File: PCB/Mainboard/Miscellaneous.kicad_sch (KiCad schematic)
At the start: 8 parts

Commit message: Update schematic and lay-out
- Swap out CP2102N, ATmega328PB and CP with new Kicad 6 symbol
- Correct all links to point to new zoudio_symbols and zoudio_footprint libraries
- Lay-out updated, only antenna is left to update.
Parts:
- LOGO1: footprint ZOUDIO-footprints:ZOUDIO25mm_mask -> zoudio_footprints:ZOUDIO25mm_mask
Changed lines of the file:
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@@
     )
     (property "Value" "ZOUDIO" (id 1) (at 172.72 101.6 0))
-    (property "Footprint" "ZOUDIO-footprints:ZOUDIO25mm_mask" (id 2) (at 172.72 95.25 0)
+    (property "Footprint" "zoudio_footprints:ZOUDIO25mm_mask" (id 2) (at 172.72 95.25 0)
       (effects (font (size 1.27 1.27)) hide)
     )

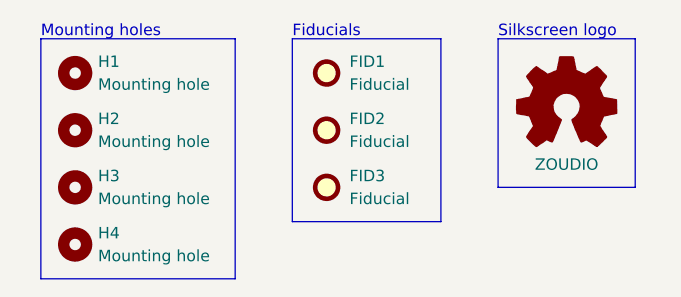
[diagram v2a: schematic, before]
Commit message: Mainboard: version 1.1.1
- No change in electrical connectivity
- Make 3D model more complete
- Improvements in paste layer for manufacturability
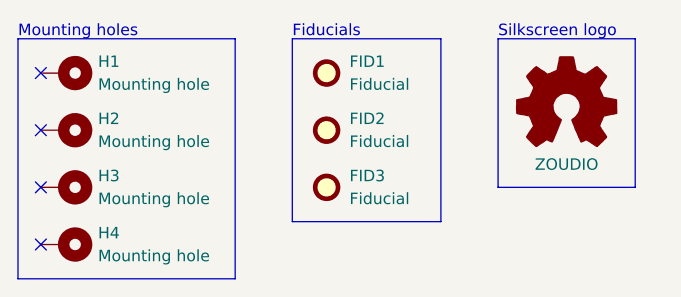
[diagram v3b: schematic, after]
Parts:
- H1, H2, H3, H4: symbol Mechanical:MountingHole -> Mechanical:MountingHole_Pad
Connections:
- no-connect marks 0 -> 4
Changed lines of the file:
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@@
   (title_block
     (title "4x38W amp with DSP and BT")
-    (date "2022-02-12")
-    (rev "1.1")
+    (date "2022-04-17")
+    (rev "1.1.1")
     (company "ZOUDIO")
   )
+  (no_connect (at 114.3 97.79))
+  (no_connect (at 114.3 91.44))
+  (no_connect (at 114.3 110.49))
+  (no_connect (at 114.3 104.14))
   (polyline (pts (xy 180.34 87.63) (xy 180.34 104.14))
     (stroke (width 0) (type default) (color 0 0 0 0))
@@
     (stroke (width 0) (type default) (color 0 0 0 0))
   )
-  (polyline (pts (xy 114.3 87.63) (xy 135.89 87.63))
+  (polyline (pts (xy 111.76 87.63) (xy 135.89 87.63))
     (stroke (width 0) (type default) (color 0 0 0 0))
   )
@@
     (stroke (width 0) (type default) (color 0 0 0 0))
   )
-  (polyline (pts (xy 135.89 114.3) (xy 114.3 114.3))
+  (polyline (pts (xy 135.89 114.3) (xy 111.76 114.3))
     (stroke (width 0) (type default) (color 0 0 0 0))
   )
@@
     (stroke (width 0) (type default) (color 0 0 0 0))
   )
-  (polyline (pts (xy 114.3 114.3) (xy 114.3 87.63))
+  (polyline (pts (xy 111.76 114.3) (xy 111.76 87.63))
     (stroke (width 0) (type default) (color 0 0 0 0))
   )
@@
     (stroke (width 0) (type default) (color 0 0 0 0))
   )
-  (text "Mounting holes" (at 114.3 87.63 0)
+  (text "Mounting holes" (at 111.76 87.63 0)
     (effects (font (size 1.27 1.27)) (justify left bottom))
   )
@@
     )
   )
-  (symbol (lib_id "Mechanical:MountingHole") (at 118.11 91.44 0) (unit 1)
+  (symbol (lib_id "Mechanical:MountingHole_Pad") (at 116.84 91.44 270) (unit 1)
     (in_bom yes) (on_board yes)
-    (property "Reference" "H1" (id 0) (at 120.65 90.17 0)
+    (property "Reference" "H1" (id 0) (at 120.65 90.17 90)
       (effects (font (size 1.27 1.27)) (justify left))
     )
-    (property "Value" "Mounting hole" (id 1) (at 120.65 92.71 0)
+    (property "Value" "Mounting hole" (id 1) (at 120.65 92.71 90)
       (effects (font (size 1.27 1.27)) (justify left))
     )
-    (property "Footprint" "MountingHole:MountingHole_3.2mm_M3_Pad_Via" (id 2) (at 118.11 91.44 0)
+    (property "Footprint" "MountingHole:MountingHole_3.2mm_M3_Pad_Via" (id 2) (at 116.84 91.44 0)
       (effects (font (size 1.27 1.27)) hide)
     )
-    (property "Datasheet" "~" (id 3) (at 118.11 91.44 0)
+    (property "Datasheet" "~" (id 3) (at 116.84 91.44 0)
       (effects (font (size 1.27 1.27)) hide)
     )
-    (property "Config" "dnp" (id 4) (at 118.11 91.44 0)
+    (property "Config" "dnp" (id 4) (at 116.84 91.44 0)
       (effects (font (size 1.27 1.27)) hide)
     )
+    (pin "1")
   )
-  (symbol (lib_id "Mechanical:MountingHole") (at 118.11 97.79 0) (unit 1)
+  (symbol (lib_id "Mechanical:MountingHole_Pad") (at 116.84 97.79 270) (unit 1)
     (in_bom yes) (on_board yes)
-    (property "Reference" "H2" (id 0) (at 120.65 96.52 0)
+    (property "Reference" "H2" (id 0) (at 120.65 96.52 90)
       (effects (font (size 1.27 1.27)) (justify left))
     )
-    (property "Value" "Mounting hole" (id 1) (at 120.65 99.06 0)
+    (property "Value" "Mounting hole" (id 1) (at 120.65 99.06 90)
       (effects (font (size 1.27 1.27)) (justify left))
     )
-    (property "Footprint" "MountingHole:MountingHole_3.2mm_M3_Pad_Via" (id 2) (at 118.11 97.79 0)
+    (property "Footprint" "MountingHole:MountingHole_3.2mm_M3_Pad_Via" (id 2) (at 116.84 97.79 0)
       (effects (font (size 1.27 1.27)) hide)
     )
-    (property "Datasheet" "~" (id 3) (at 118.11 97.79 0)
+    (property "Datasheet" "~" (id 3) (at 116.84 97.79 0)
       (effects (font (size 1.27 1.27)) hide)
     )
-    (property "Config" "dnp" (id 4) (at 118.11 97.79 0)
+    (property "Config" "dnp" (id 4) (at 116.84 97.79 0)
       (effects (font (size 1.27 1.27)) hide)
     )
+    (pin "1")
   )
-  (symbol (lib_id "Mechanical:MountingHole") (at 118.11 104.14 0) (unit 1)
+  (symbol (lib_id "Mechanical:MountingHole_Pad") (at 116.84 104.14 270) (unit 1)
     (in_bom yes) (on_board yes)
-    (property "Reference" "H3" (id 0) (at 120.65 102.87 0)
+    (property "Reference" "H3" (id 0) (at 120.65 102.87 90)
       (effects (font (size 1.27 1.27)) (justify left))
     )
-    (property "Value" "Mounting hole" (id 1) (at 120.65 105.41 0)
+    (property "Value" "Mounting hole" (id 1) (at 120.65 105.41 90)
       (effects (font (size 1.27 1.27)) (justify left))
     )
-    (property "Footprint" "MountingHole:MountingHole_3.2mm_M3_Pad_Via" (id 2) (at 118.11 104.14 0)
+    (property "Footprint" "MountingHole:MountingHole_3.2mm_M3_Pad_Via" (id 2) (at 116.84 104.14 0)
       (effects (font (size 1.27 1.27)) hide)
     )
-    (property "Datasheet" "~" (id 3) (at 118.11 104.14 0)
+    (property "Datasheet" "~" (id 3) (at 116.84 104.14 0)
       (effects (font (size 1.27 1.27)) hide)
     )
-    (property "Config" "dnp" (id 4) (at 118.11 104.14 0)
+    (property "Config" "dnp" (id 4) (at 116.84 104.14 0)
       (effects (font (size 1.27 1.27)) hide)
     )
+    (pin "1")
   )
-  (symbol (lib_id "Mechanical:MountingHole") (at 118.11 110.49 0) (unit 1)
+  (symbol (lib_id "Mechanical:MountingHole_Pad") (at 116.84 110.49 270) (unit 1)
     (in_bom yes) (on_board yes)
-    (property "Reference" "H4" (id 0) (at 120.65 109.22 0)
+    (property "Reference" "H4" (id 0) (at 120.65 109.22 90)
       (effects (font (size 1.27 1.27)) (justify left))
     )
-    (property "Value" "Mounting hole" (id 1) (at 120.65 111.76 0)
+    (property "Value" "Mounting hole" (id 1) (at 120.65 111.76 90)
       (effects (font (size 1.27 1.27)) (justify left))
     )
-    (property "Footprint" "MountingHole:MountingHole_3.2mm_M3_Pad_Via" (id 2) (at 118.11 110.49 0)
+    (property "Footprint" "MountingHole:MountingHole_3.2mm_M3_Pad_Via" (id 2) (at 116.84 110.49 0)
       (effects (font (size 1.27 1.27)) hide)
     )
-    (property "Datasheet" "~" (id 3) (at 118.11 110.49 0)
+    (property "Datasheet" "~" (id 3) (at 116.84 110.49 0)
       (effects (font (size 1.27 1.27)) hide)
     )
-    (property "Config" "dnp" (id 4) (at 118.11 110.49 0)
+    (property "Config" "dnp" (id 4) (at 116.84 110.49 0)
       (effects (font (size 1.27 1.27)) hide)
     )
+    (pin "1")
   )
   (symbol (lib_id "Graphic:Logo_Open_Hardware_Small") (at 172.72 95.25 0) (unit 1)

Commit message: Mainboard: version 1.1.2
Add testpoints for power rail testing
Move backside info and logo from mask to silkscreen
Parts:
- LOGO1: footprint zoudio_footprints:ZOUDIO25mm_mask -> zoudio_footprints:ZOUDIO25mm
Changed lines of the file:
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@@
   (title_block
     (title "4x38W amp with DSP and BT")
-    (date "2022-04-17")
-    (rev "1.1.1")
+    (date "2022-04-29")
+    (rev "1.1.2")
     (company "ZOUDIO")
   )
@@
     )
     (property "Value" "ZOUDIO" (id 1) (at 172.72 101.6 0))
-    (property "Footprint" "zoudio_footprints:ZOUDIO25mm_mask" (id 2) (at 172.72 95.25 0)
+    (property "Footprint" "zoudio_footprints:ZOUDIO25mm" (id 2) (at 172.72 95.25 0)
       (effects (font (size 1.27 1.27)) hide)
     )
